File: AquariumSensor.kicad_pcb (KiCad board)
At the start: 2 copper layers, 42 x 60 mm, 13 parts, among them J3 Barrel_Jack, SW1 SW_Reed, SW2 SW_Reed

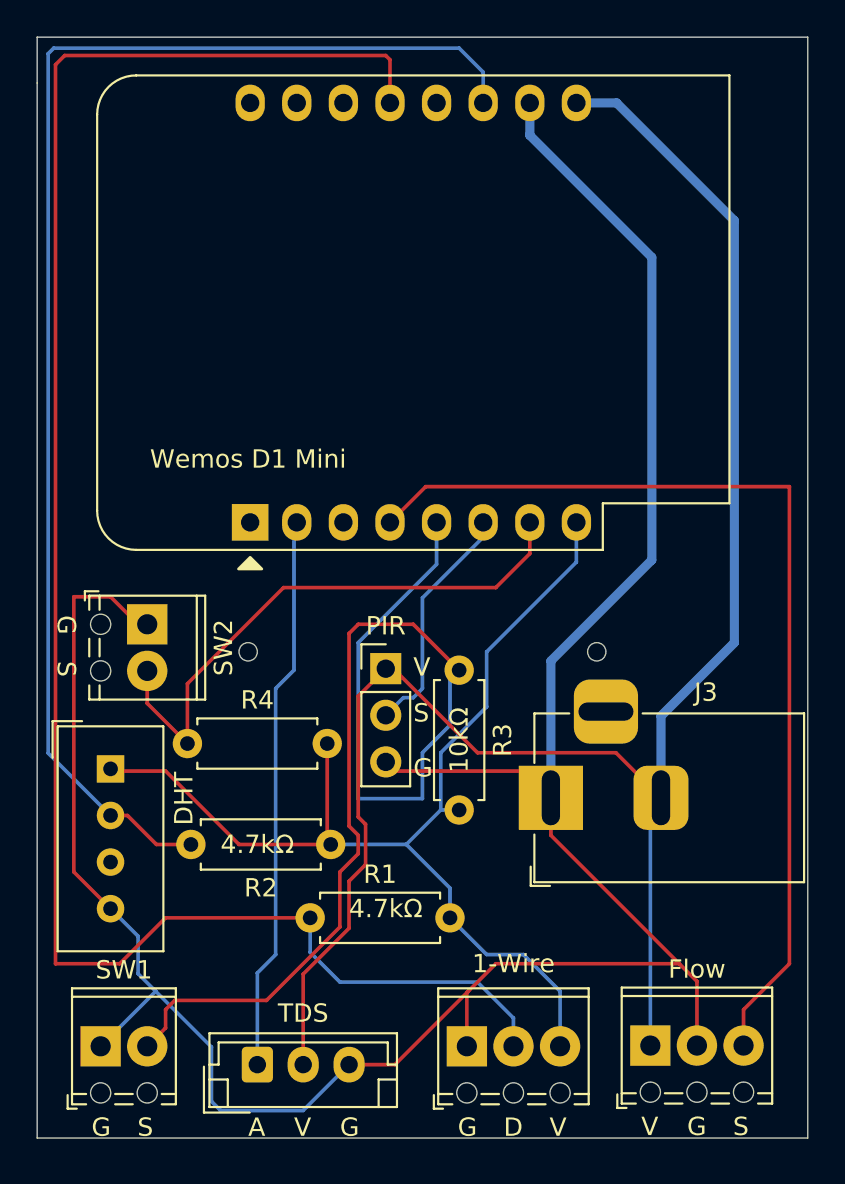
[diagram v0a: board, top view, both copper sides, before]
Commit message: 1.1 Release to fix wrong polarity on J3 DC Jack
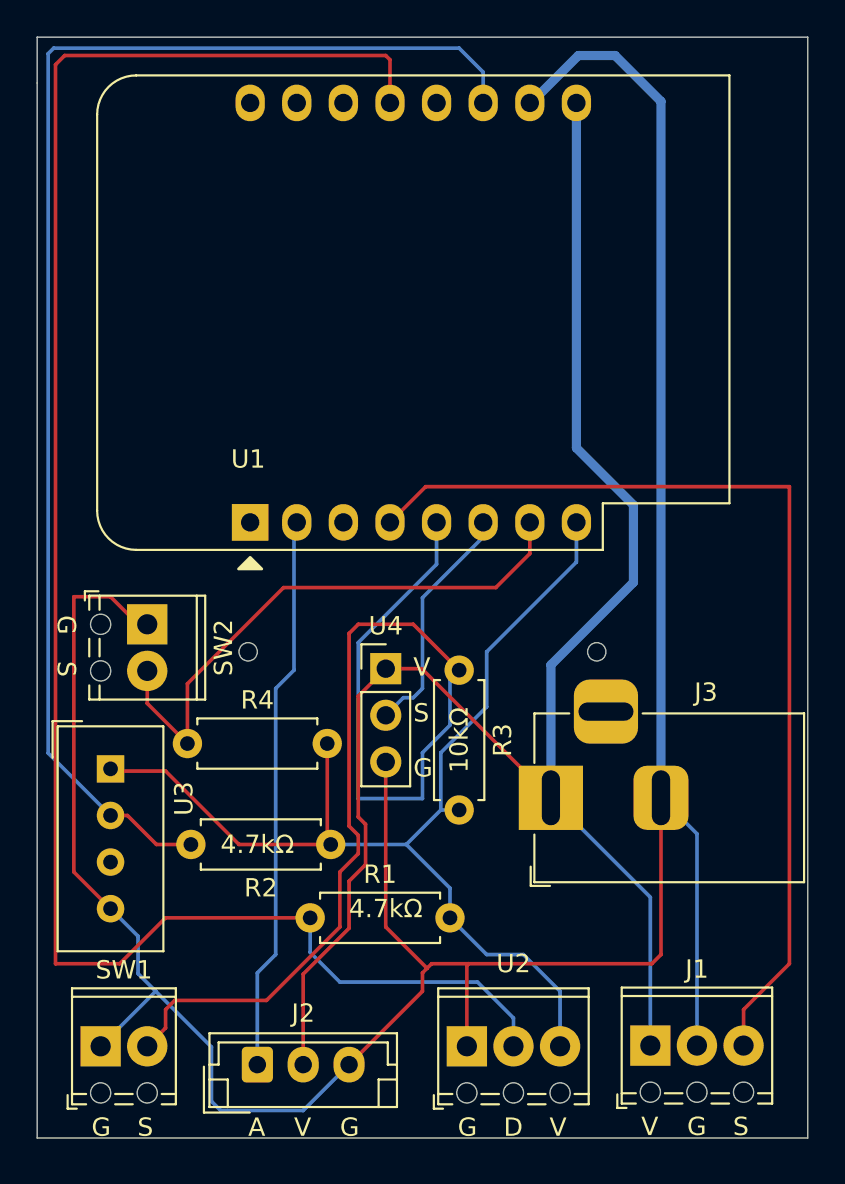
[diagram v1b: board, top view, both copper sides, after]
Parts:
- U1: renamed from Wemos D1 Mini
- renumbered Flow to J1, TDS to J2, 1-Wire to U2, DHT to U3, PIR to U4
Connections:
- J3 pad 1: Net-(J1-GND) -> Net-(J1-VCC)
- J3 pad 2: Net-(J1-VCC) -> Net-(J1-GND)
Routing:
- net Net-(J1-GND): track 141.1 -> 154.5 mm
- net Net-(J1-VCC): track 99.8 -> 92.5 mm
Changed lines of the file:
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@@
 	(net 11 "Net-(J1-Signal)")
 	(net 12 "Net-(J1-GND)")
-	(net 13 "Net-(J2-VCC)")
+	(net 13 "Net-(J2-AOUT)")
 	(net 14 "Net-(U1-D4)")
 	(net 15 "unconnected-(U3-NC-Pad3)")
@@
 		(descr "Terminal Block Phoenix MPT-0,5-3-2.54, 3 pins, pitch 2.54mm, size 8.08x6.2mm^2, drill diamater 1.1mm, pad diameter 2.2mm, see http://www.mouser.com/ds/2/324/ItemDetail_1725656-920552.pdf, script-generated using https://github.com/pointhi/kicad-footprint-generator/scripts/TerminalBlock_Phoenix")
 		(tags "THT Terminal Block Phoenix MPT-0,5-3-2.54 pitch 2.54mm size 8.08x6.2mm^2 drill 1.1mm pad 2.2mm")
-		(property "Reference" "Flow"
+		(property "Reference" "J1"
 			(at 2.54 -4.16 0)
 			(layer "F.SilkS")
@@
 			(layers "*.Cu" "*.Mask")
 			(remove_unused_layers no)
-			(net 12 "Net-(J1-GND)")
+			(net 10 "Net-(J1-VCC)")
 			(pintype "passive")
 		)
@@
 			(remove_unused_layers no)
 			(roundrect_rratio 0.25)
-			(net 10 "Net-(J1-VCC)")
+			(net 12 "Net-(J1-GND)")
 			(pintype "passive")
 		)
@@
 		(descr "JST EH series connector, B3B-EH-A (http://www.jst-mfg.com/product/pdf/eng/eEH.pdf), generated with kicad-footprint-generator")
 		(tags "connector JST EH vertical")
-		(property "Reference" "TDS"
+		(property "Reference" "J2"
 			(at 2.5 -2.8 0)
 			(layer "F.SilkS")
@@
 			(remove_unused_layers no)
 			(roundrect_rratio 0.147059)
-			(net 13 "Net-(J2-VCC)")
+			(net 13 "Net-(J2-AOUT)")
 			(pinfunction "AOUT")
 			(pintype "output")
@@
 		(descr "Through hole straight pin header, 1x03, 2.54mm pitch, single row")
 		(tags "Through hole pin header THT 1x03 2.54mm single row")
-		(property "Reference" "PIR"
+		(property "Reference" "U4"
 			(at 0 -2.33 0)
 			(layer "F.SilkS")
@@
 		(descr "Terminal Block Phoenix MPT-0,5-3-2.54, 3 pins, pitch 2.54mm, size 8.08x6.2mm^2, drill diamater 1.1mm, pad diameter 2.2mm, see http://www.mouser.com/ds/2/324/ItemDetail_1725656-920552.pdf, script-generated using https://github.com/pointhi/kicad-footprint-generator/scripts/TerminalBlock_Phoenix")
 		(tags "THT Terminal Block Phoenix MPT-0,5-3-2.54 pitch 2.54mm size 8.08x6.2mm^2 drill 1.1mm pad 2.2mm")
-		(property "Reference" "1-Wire"
+		(property "Reference" "U2"
 			(at 2.54 -4.5 0)
 			(layer "F.SilkS")
@@
 		(descr "16-pin module, column spacing 22.86 mm (900 mils), https://wiki.wemos.cc/products:d1:d1_mini, https://c1.staticflickr.com/1/734/31400410271_f278b087db_z.jpg")
 		(tags "ESP8266 WiFi microcontroller")
-		(property "Reference" "Wemos D1 Mini"
+		(property "Reference" "U1"
 			(at 3.445 -0.11 0)
 			(layer "F.SilkS")
@@
 			(layers "*.Cu" "*.Mask")
 			(remove_unused_layers no)
-			(net 13 "Net-(J2-VCC)")
+			(net 13 "Net-(J2-AOUT)")
 			(pinfunction "A0")
 			(pintype "input")
@@
 		)
 		(fp_text user "S"
-			(at 2 5 270)
+			(at 2 5 -90)
 			(unlocked yes)
 			(layer "F.SilkS")
@@
 		(descr "Temperature and humidity module, http://akizukidenshi.com/download/ds/aosong/DHT11.pdf")
 		(tags "Temperature and humidity module")
-		(property "Reference" "DHT"
+		(property "Reference" "U3"
 			(at 4 1.62 90)
 			(layer "F.SilkS")
@@
 	)
 	(segment
-		(start 76.5425 101)
-		(end 79 103.4575)
-		(width 0.2)
-		(layer "F.Cu")
-		(net 10)
-	)
-	(segment
 		(start 62 108)
 		(end 62 110.565686)
@@
 	(segment
 		(start 64 96.42)
-		(end 64.42 96.42)
+		(end 65.9625 96.42)
 		(width 0.2)
 		(layer "F.Cu")
@@
 	)
 	(segment
-		(start 69 101)
-		(end 76.5425 101)
-		(width 0.2)
-		(layer "F.Cu")
-		(net 10)
-	)
-	(segment
 		(start 62.9 104.9)
 		(end 62.9 107.1)
@@
 	)
 	(segment
-		(start 64.42 96.42)
-		(end 69 101)
+		(start 59.5 113.065686)
+		(end 59.5 118)
 		(width 0.2)
 		(layer "F.Cu")
@@
 	)
 	(segment
-		(start 59.5 113.065686)
-		(end 59.5 118)
+		(start 65.9625 96.42)
+		(end 73 103.4575)
 		(width 0.2)
 		(layer "F.Cu")
@@
 	)
 	(segment
-		(start 83 95)
-		(end 83 72)
-		(width 0.5)
+		(start 78.42 108.8775)
+		(end 73 103.4575)
+		(width 0.2)
 		(layer "B.Cu")
 		(net 10)
 	)
 	(segment
-		(start 76.585 65.585)
-		(end 74.39 65.585)
-		(width 0.5)
+		(start 78.42 116.96)
+		(end 78.42 108.8775)
+		(width 0.2)
 		(layer "B.Cu")
 		(net 10)
 	)
 	(segment
-		(start 79 99)
-		(end 83 95)
+		(start 73 96.215106)
+		(end 73 103.4575)
 		(width 0.5)
 		(layer "B.Cu")
@@
 	)
 	(segment
-		(start 79 103.4575)
-		(end 79 103)
-		(width 0.2)
-		(layer "B.Cu")
-		(net 10)
-	)
-	(segment
-		(start 79 103)
-		(end 79 99)
+		(start 77.5 91.715106)
+		(end 73 96.215106)
 		(width 0.5)
 		(layer "B.Cu")
@@
 	)
 	(segment
-		(start 83 72)
-		(end 76.585 65.585)
+		(start 77.5 87.5)
+		(end 77.5 91.715106)
 		(width 0.5)
 		(layer "B.Cu")
@@
 	)
 	(segment
-		(start 78.42 104.0375)
-		(end 79 103.4575)
-		(width 0.2)
+		(start 74.39 84.39)
+		(end 77.5 87.5)
+		(width 0.5)
 		(layer "B.Cu")
 		(net 10)
 	)
 	(segment
-		(start 78.42 116.96)
-		(end 78.42 104.0375)
-		(width 0.2)
+		(start 74.39 65.585)
+		(end 74.39 84.39)
+		(width 0.5)
 		(layer "B.Cu")
 		(net 10)
@@
 	)
 	(segment
-		(start 80.96 113.46)
-		(end 80.96 116.96)
+		(start 66.25 112.75)
+		(end 66.5 112.5)
 		(width 0.2)
 		(layer "F.Cu")
@@
 	)
 	(segment
-		(start 68.42 114.08)
-		(end 68.5 114)
-		(width 0.2)
-		(layer "F.Cu")
-		(net 12)
-	)
-	(segment
-		(start 72.5 112.5)
-		(end 80 112.5)
-		(width 0.2)
-		(layer "F.Cu")
-		(net 12)
-	)
-	(segment
-		(start 68.5 114)
-		(end 70 112.5)
+		(start 62 118)
+		(end 66 114)
 		(width 0.2)
 		(layer "F.Cu")
@@
 	)
 	(segment
-		(start 47 107.5)
-		(end 49 109.5)
+		(start 64 101.5)
+		(end 64 110.5)
 		(width 0.2)
 		(layer "F.Cu")
@@
 	)
 	(segment
-		(start 50.5 94)
-		(end 49 92.5)
+		(start 66.5 112.5)
+		(end 68.5 112.5)
 		(width 0.2)
 		(layer "F.Cu")
@@
 	)
 	(segment
-		(start 49 92.5)
-		(end 47 92.5)
+		(start 66 114)
+		(end 66 113)
 		(width 0.2)
 		(layer "F.Cu")
@@
 	)
 	(segment
-		(start 68.42 117)
-		(end 68.42 114.08)
+		(start 47 107.5)
+		(end 49 109.5)
 		(width 0.2)
 		(layer "F.Cu")
@@
 	)
 	(segment
-		(start 64.5 118)
-		(end 68.5 114)
+		(start 50.5 94)
+		(end 49 92.5)
 		(width 0.2)
 		(layer "F.Cu")
@@
 	)
 	(segment
-		(start 73 103.4575)
-		(end 73 105.5)
+		(start 64 110.5)
+		(end 66.25 112.75)
 		(width 0.2)
 		(layer "F.Cu")
@@
 	)
 	(segment
-		(start 62 118)
-		(end 64.5 118)
+		(start 68.42 112.58)
+		(end 68.5 112.5)
 		(width 0.2)
 		(layer "F.Cu")
@@
 	)
 	(segment
-		(start 64.5 102)
-		(end 71.5425 102)
+		(start 49 92.5)
+		(end 47 92.5)
 		(width 0.2)
 		(layer "F.Cu")
@@
 	)
 	(segment
-		(start 80 112.5)
-		(end 80.96 113.46)
+		(start 68.5 112.5)
+		(end 78.5 112.5)
 		(width 0.2)
 		(layer "F.Cu")
@@
 	)
 	(segment
-		(start 71.5425 102)
-		(end 73 103.4575)
+		(start 78.5 112.5)
+		(end 79 112)
 		(width 0.2)
 		(layer "F.Cu")
@@
 	)
 	(segment
-		(start 73 105.5)
-		(end 80 112.5)
+		(start 68.42 117)
+		(end 68.42 112.58)
 		(width 0.2)
 		(layer "F.Cu")
@@
 	)
 	(segment
-		(start 64 101.5)
-		(end 64.5 102)
+		(start 66 113)
+		(end 66.25 112.75)
 		(width 0.2)
 		(layer "F.Cu")
@@
 	)
 	(segment
-		(start 70 112.5)
-		(end 72.5 112.5)
+		(start 79 112)
+		(end 79 103.4575)
 		(width 0.2)
 		(layer "F.Cu")
@@
 	)
 	(segment
-		(start 73 103.4575)
-		(end 73 96)
+		(start 71.915 65.585)
+		(end 74.5 63)
 		(width 0.5)
 		(layer "B.Cu")
@@
 	)
 	(segment
-		(start 71.85 67.35)
-		(end 71.85 65.585)
-		(width 0.5)
-		(layer "B.Cu")
-		(net 12)
-	)
-	(segment
 		(start 51.46 114)
 		(end 48.46 117)
@@
 	)
 	(segment
-		(start 78.5 90.5)
-		(end 78.5 74)
+		(start 74.5 63)
+		(end 76.5 63)
 		(width 0.5)
 		(layer "B.Cu")
@@
 	)
 	(segment
-		(start 73 96)
-		(end 78.5 90.5)
-		(width 0.5)
+		(start 80.96 116.96)
+		(end 80.96 105.4175)
+		(width 0.2)
+		(layer "B.Cu")
+		(net 12)
+	)
+	(segment
+		(start 80.96 105.4175)
+		(end 79 103.4575)
+		(width 0.2)
 		(layer "B.Cu")
 		(net 12)
@@
 	)
 	(segment
-		(start 78.5 74)
-		(end 71.85 67.35)
+		(start 76.5 63)
+		(end 79 65.5)
 		(width 0.5)
 		(layer "B.Cu")
@@
 		(layer "B.Cu")
 		(net 12)
+	)
+	(segment
+		(start 71.85 65.585)
+		(end 71.915 65.585)
+		(width 0.5)
+		(layer "B.Cu")
+		(net 12)
+	)
+	(segment
+		(start 79 65.5)
+		(end 79 102.9075)
+		(width 0.5)
+		(layer "B.Cu")
+		(net 12)
